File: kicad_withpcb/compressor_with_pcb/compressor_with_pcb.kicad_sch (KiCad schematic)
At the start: 167 parts, among them J1 EDA 306, J2 FRONT BOARD, Q1 BC549C, Q2 BC549C, Q3 BC549C, Q4 BC549C, Q5 BC549C, Q6 BC549C, Q7 BC549C, Q8 BC549C, Q9 BC549C, SW1 BYPASS, SW2 INT/EXT, SW3 HPF DEFEAT, SW4 LINK, U1 NE5532, U10 LM3915, U2 NE5532, U3 NE5532, U4 TL072, U5 NE5532, U6 NE5532, U7 NE5532, U9 LM3914

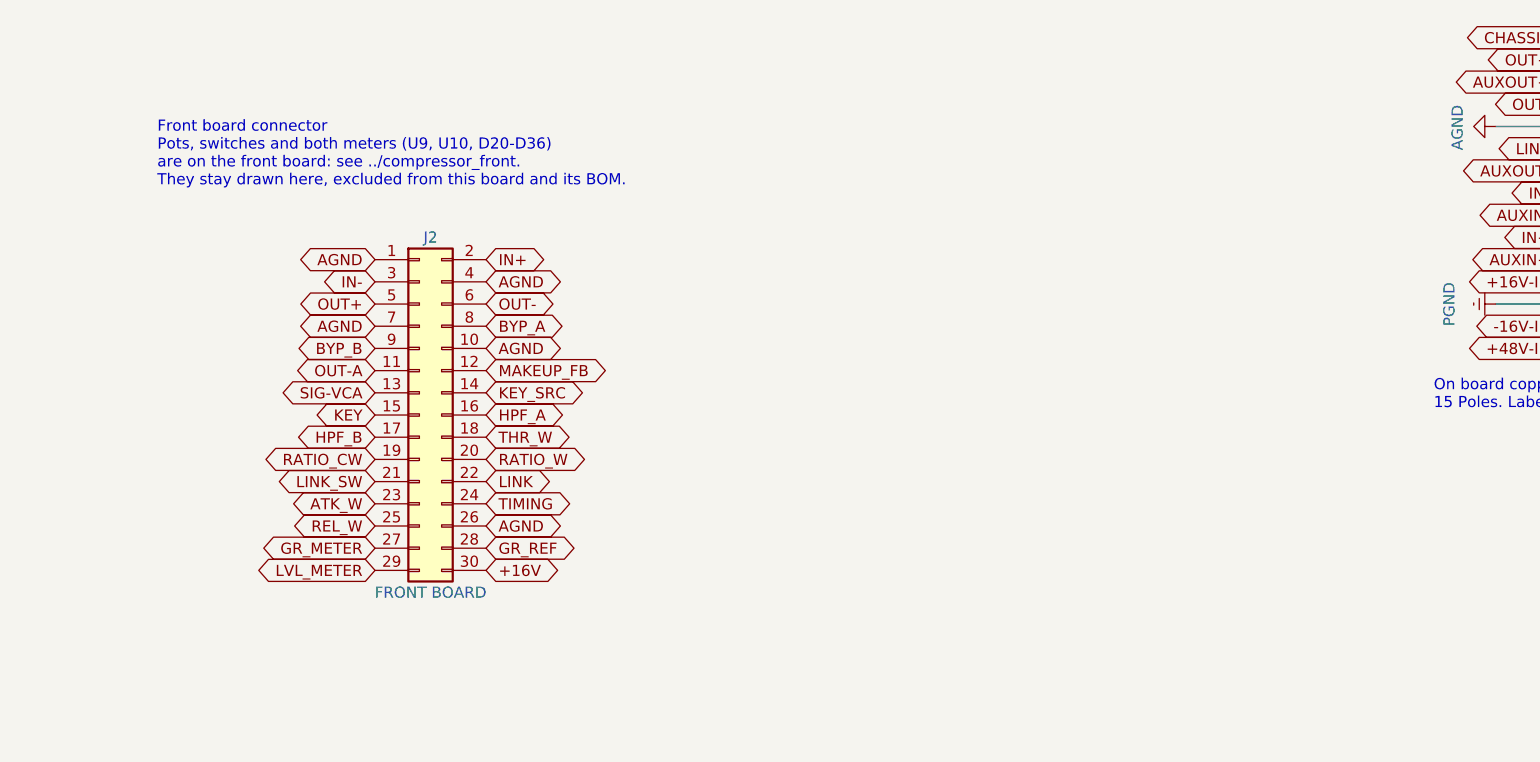
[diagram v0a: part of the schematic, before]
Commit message: Put the op amps in sockets
U1 to U7 use the DIP-8 socket footprint. The pads are the same, so the
routing and pour are untouched; only the outlines grow. References moved back
inside them.

DRC unchanged: 0 errors, 0 unconnected, parity clean.

Co-Authored-By: Claude Opus 5.5 (1M context) <noreply@anthropic.com>
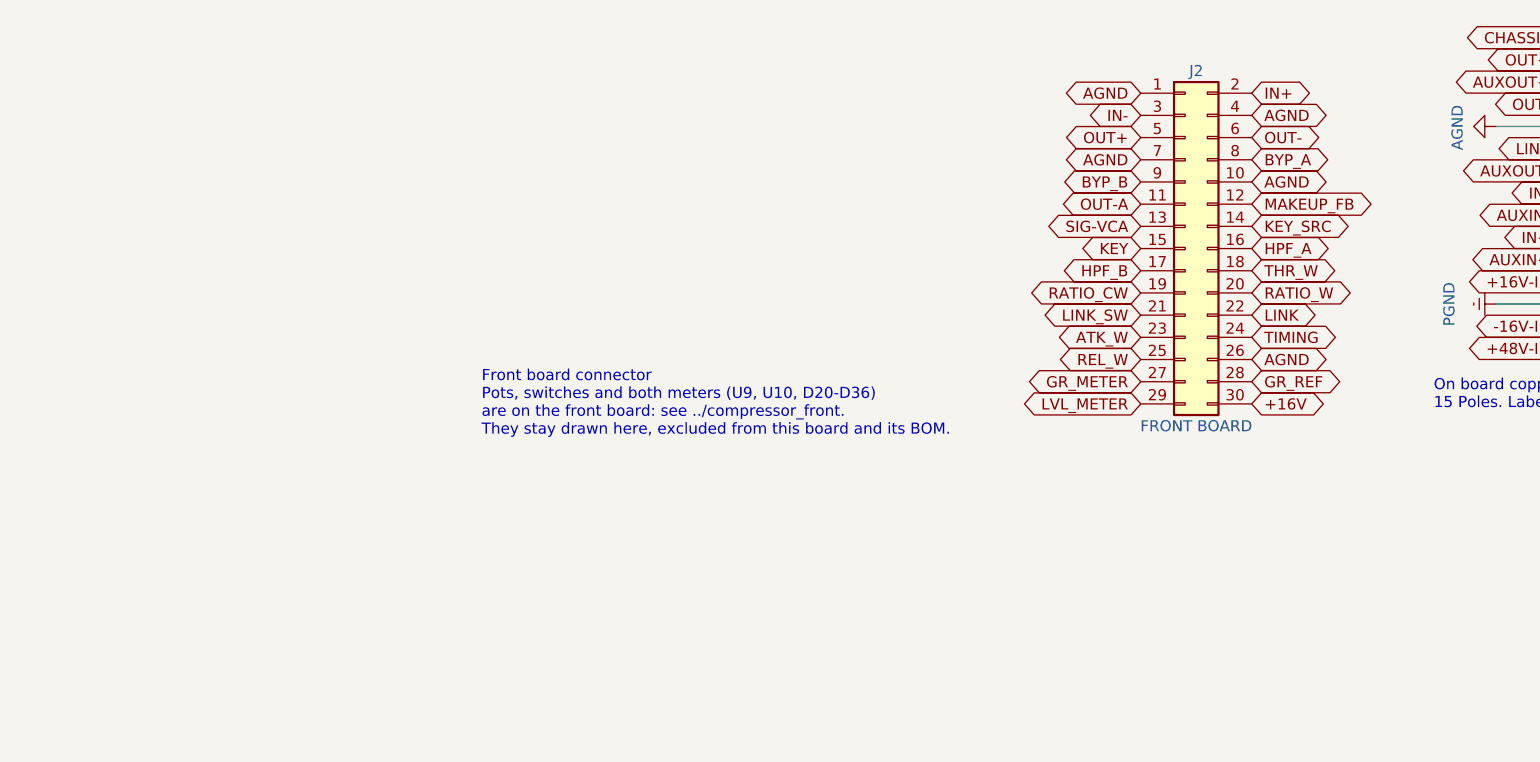
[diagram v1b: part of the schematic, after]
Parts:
- U1, U2, U3, U4, U5, U6, U7: footprint Package_DIP:DIP-8_W7.62mm -> Package_DIP:DIP-8_W7.62mm_Socket
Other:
- moved on the sheet: J2
